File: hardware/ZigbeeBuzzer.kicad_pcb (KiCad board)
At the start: 2 copper layers, 26 x 21 mm, 14 parts, among them Q1 NPN, U1 Xiao-ESP32-C6

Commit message: Added diode
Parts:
- added D1: CUS08F30, Medo64:D Shottky (SOD123F), B.Cu at (41.5, 29.3)
- moved S1 1.50 mm to (41.5, 35.5)
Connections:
- U1 pad 10: (no net) -> BUTTON
- U1 pad 11: BUTTON -> (no net)
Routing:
- net BEEPER: track 18.0 -> 29.5 mm
- net GND: track 65.3 -> 71.3 mm, vias 1 -> 2
- net 3V3: track 39.7 -> 41.9 mm
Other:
- outline, holes or cut-outs redrawn

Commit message: Added PCB designator
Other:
- board text added: "ZigbeeBuzzer AXXXX"
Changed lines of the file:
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@@
 		(layer "F.Fab")
+	)
+	(gr_text "ZigbeeBuzzer AXXXX"
+		(at 33 33 0)
+		(layer "B.SilkS")
+		(effects
+			(font
+				(size 0.8 0.6)
+				(thickness 0.15)
+				(bold yes)
+			)
+			(justify mirror)
+		)
 	)
 	(segment

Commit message: Added polarity marking to beeper
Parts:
- turned LS1 to 90 degrees
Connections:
- LS1 pad 1: 3V3 -> BEEPER
- LS1 pad 2: BEEPER -> 3V3
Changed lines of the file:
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@@
 	(footprint "Medo64:LS Buzzer (D9.5-H5.5)"
 		(layer "B.Cu")
-		(at 33 26 -90)
+		(at 33 26 90)
 		(property "Reference" "LS1"
 			(at 0 0 0)
@@
 			(layer "B.Fab")
 		)
-		(pad "1" thru_hole circle
-			(at -2.5 0 270)
+		(fp_text user "+"
+			(at 2.5 1 90)
+			(layer "B.SilkS")
+			(effects
+				(font
+					(size 0.8 0.6)
+					(thickness 0.15)
+					(bold yes)
+				)
+				(justify top mirror)
+			)
+		)
+		(pad "1" thru_hole roundrect
+			(at -2.5 0 90)
+			(size 1.4 1.4)
+			(drill 0.8)
+			(layers "*.Cu" "*.Mask")
+			(remove_unused_layers no)
+			(roundrect_rratio 0.25)
+			(chamfer_ratio 0.2)
+			(chamfer top_left bottom_left)
+			(net 7 "BEEPER")
+		)
+		(pad "2" thru_hole circle
+			(at 2.5 0 90)
 			(size 1.4 1.4)
 			(drill 0.8)
@@
 			(net 8 "3V3")
 		)
-		(pad "2" thru_hole circle
-			(at 2.5 0 270)
-			(size 1.4 1.4)
-			(drill 0.8)
-			(layers "*.Cu" "*.Mask")
-			(remove_unused_layers no)
-			(net 7 "BEEPER")
-		)
 		(embedded_fonts no)

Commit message: Refactoring button location
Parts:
- moved DS1 13.5 mm to (33.0, 32.5), turned to 0 degrees
- moved S1 11.0 mm to (41.5, 24.5), turned to 90 degrees
- moved R4 10.7 mm to (41.5, 35.2), turned to 0 degrees
- moved D1 3.40 mm to (41.5, 32.7), turned to 180 degrees
- moved C2 3.40 mm to (41.5, 30.2)
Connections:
- R4 pad 1: (no net) -> OUT_LED
- U1 pad 9: (no net) -> OUT_LED
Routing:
- net LED: track 2.45 -> 9.60 mm
- net BUTTON: track 9.12 -> 16.1 mm
- net GND: track 71.3 -> 67.6 mm
- net BEEPER: track 29.5 -> 26.7 mm
- net OUT_LED: track 0.00 -> 2.71 mm, vias 0 -> 1
- net 3V3: track 41.9 -> 40.2 mm

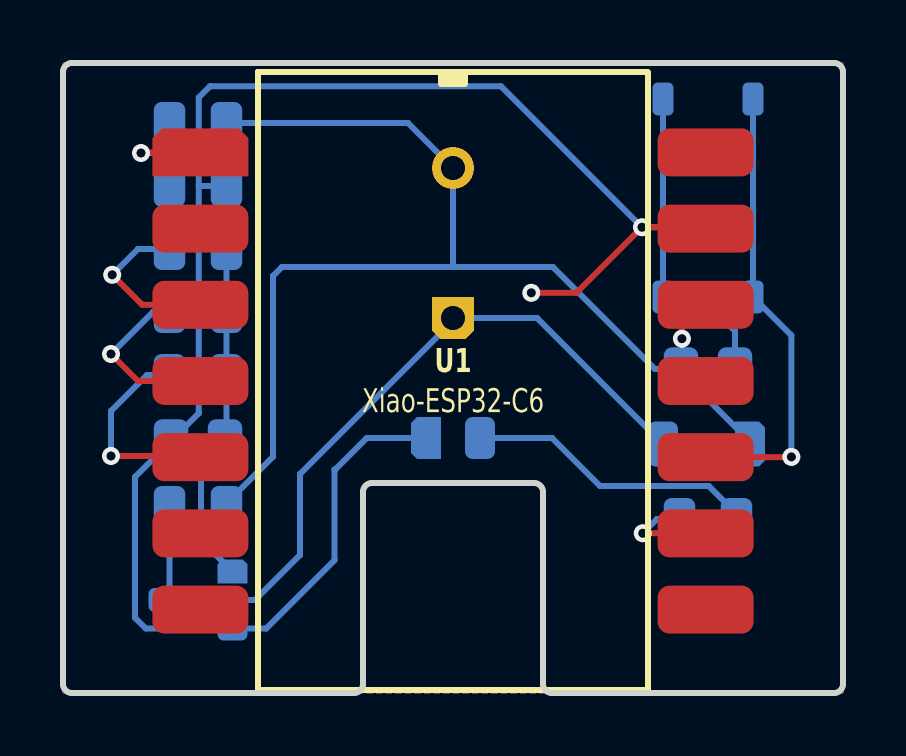
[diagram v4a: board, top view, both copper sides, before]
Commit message: Updated buzzer footprint
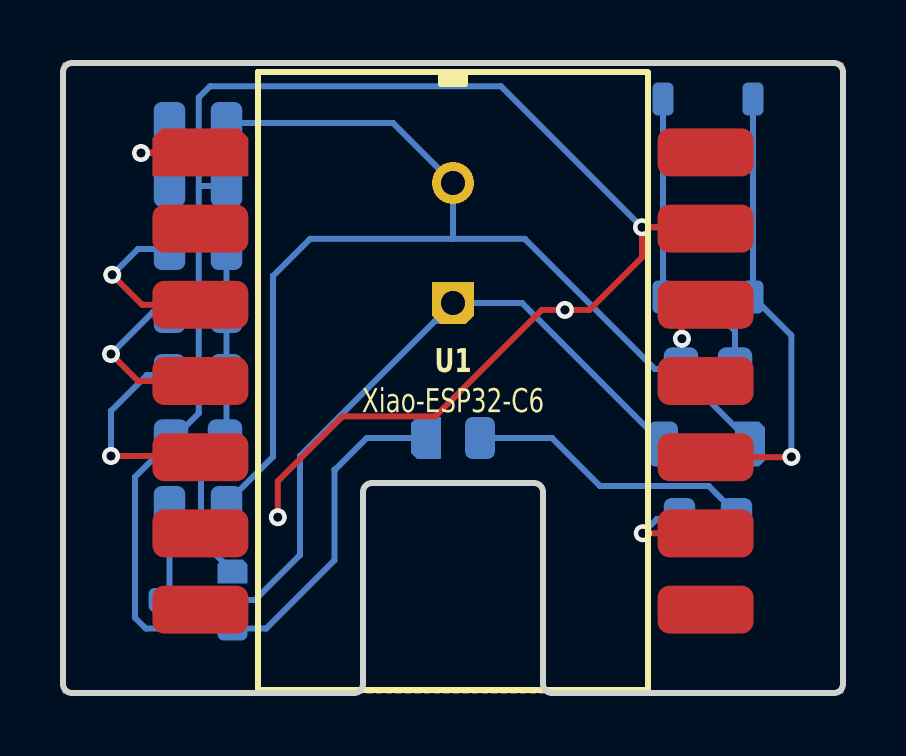
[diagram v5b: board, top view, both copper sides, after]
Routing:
- net GND: track 67.6 -> 80.4 mm, vias 2 -> 3
- net BEEPER: track 26.7 -> 27.3 mm
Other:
- board text added: "ZigbeeBuzzer BXXXX"
- board text removed: "ZigbeeBuzzer AXXXX"
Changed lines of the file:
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@@
 		(fp_circle
 			(center 0 0)
-			(end 4.6 0)
+			(end 4.4 0)
 			(stroke
 				(width 0.2)
@@
 		)
 		(pad "1" thru_hole roundrect
-			(at -2.5 0 90)
+			(at -2 0 90)
 			(size 1.4 1.4)
 			(drill 0.8)
@@
 		)
 		(pad "2" thru_hole circle
-			(at 2.5 0 90)
+			(at 2 0 90)
 			(size 1.4 1.4)
 			(drill 0.8)
@@
 		(model "${KICAD9_3DMODEL_DIR}/Buzzer_Beeper.3dshapes/Buzzer_15x7.5RM7.6.step"
 			(offset
-				(xyz -2.5 0 0)
+				(xyz -2 0 0)
 			)
 			(scale
-				(xyz 0.65 0.65 0.75)
+				(xyz 0.5 0.5 0.75)
 			)
 			(rotate
@@
 		(layer "F.Fab")
 	)
-	(gr_text "ZigbeeBuzzer AXXXX"
+	(gr_text "ZigbeeBuzzer BXXXX"
 		(at 29.1 35.8 90)
 		(layer "B.SilkS")
@@
 	)
 	(segment
+		(start 39.3 26.48)
+		(end 37.55 28.23)
+		(width 0.2)
+		(layer "F.Cu")
+		(net 1)
+	)
+	(segment
+		(start 36.73 28.23)
+		(end 35.96 28.23)
+		(width 0.2)
+		(layer "F.Cu")
+		(net 1)
+	)
+	(segment
+		(start 37.55 28.23)
+		(end 36.73 28.23)
+		(width 0.2)
+		(layer "F.Cu")
+		(net 1)
+	)
+	(segment
+		(start 27.16 33.94)
+		(end 27.16 35.14)
+		(width 0.2)
+		(layer "F.Cu")
+		(net 1)
+	)
+	(segment
 		(start 39.3 25.475)
-		(end 37.115 27.66)
+		(end 39.3 26.48)
+		(width 0.2)
+		(layer "F.Cu")
+		(net 1)
+	)
+	(segment
+		(start 29.32 31.78)
+		(end 27.16 33.94)
+		(width 0.2)
+		(layer "F.Cu")
+		(net 1)
+	)
+	(segment
+		(start 35.96 28.23)
+		(end 32.41 31.78)
+		(width 0.2)
+		(layer "F.Cu")
+		(net 1)
+	)
+	(segment
+		(start 32.41 31.78)
+		(end 29.32 31.78)
 		(width 0.2)
 		(layer "F.Cu")
@@
 		(start 39.3 25.475)
 		(end 40.575 25.475)
-		(width 0.2)
-		(layer "F.Cu")
-		(net 1)
-	)
-	(segment
-		(start 37.115 27.66)
-		(end 35.61 27.66)
 		(width 0.2)
 		(layer "F.Cu")
@@
 	)
 	(via
-		(at 35.61 27.66)
+		(at 27.16 35.14)
+		(size 0.6)
+		(drill 0.3)
+		(layers "F.Cu" "B.Cu")
+		(net 1)
+	)
+	(via
+		(at 36.73 28.23)
 		(size 0.6)
 		(drill 0.3)
@@
 	)
 	(segment
-		(start 40 32.7)
-		(end 35.8 28.5)
+		(start 27.9 36.4)
+		(end 27.9 33.1)
+		(width 0.2)
+		(layer "B.Cu")
+		(net 7)
+	)
+	(segment
+		(start 35.3 28)
+		(end 33 28)
+		(width 0.2)
+		(layer "B.Cu")
+		(net 7)
+	)
+	(segment
+		(start 27.9 33.1)
+		(end 32.4 28.6)
 		(width 0.2)
 		(layer "B.Cu")
@@
 	)
 	(segment
+		(start 32.4 28.6)
+		(end 33 28.6)
+		(width 0.2)
+		(layer "B.Cu")
+		(net 7)
+	)
+	(segment
+		(start 23.55 34.8)
+		(end 23.55 37.7)
+		(width 0.2)
+		(layer "B.Cu")
+		(net 7)
+	)
+	(segment
+		(start 40 32.7)
+		(end 35.3 28)
+		(width 0.2)
+		(layer "B.Cu")
+		(net 7)
+	)
+	(segment
 		(start 23.35 37.9)
 		(end 26.4 37.9)
-		(width 0.2)
-		(layer "B.Cu")
-		(net 7)
-	)
-	(segment
-		(start 35.8 28.5)
-		(end 33 28.5)
-		(width 0.2)
-		(layer "B.Cu")
-		(net 7)
-	)
-	(segment
-		(start 27.9 33.7)
-		(end 33 28.6)
-		(width 0.2)
-		(layer "B.Cu")
-		(net 7)
-	)
-	(segment
-		(start 27.9 36.4)
-		(end 27.9 33.7)
-		(width 0.2)
-		(layer "B.Cu")
-		(net 7)
-	)
-	(segment
-		(start 23.55 34.8)
-		(end 23.55 37.7)
 		(width 0.2)
 		(layer "B.Cu")
@@
 	)
 	(segment
+		(start 35.39 25.86)
+		(end 33 25.86)
+		(width 0.2)
+		(layer "B.Cu")
+		(net 8)
+	)
+	(segment
+		(start 39.73 30.2)
+		(end 35.39 25.86)
+		(width 0.2)
+		(layer "B.Cu")
+		(net 8)
+	)
+	(segment
+		(start 27 33.125)
+		(end 27 27.1)
+		(width 0.2)
+		(layer "B.Cu")
+		(net 8)
+	)
+	(segment
+		(start 40.6 30.2)
+		(end 39.73 30.2)
+		(width 0.2)
+		(layer "B.Cu")
+		(net 8)
+	)
+	(segment
+		(start 27 27.1)
+		(end 28.24 25.86)
+		(width 0.2)
+		(layer "B.Cu")
+		(net 8)
+	)
+	(segment
+		(start 31 22)
+		(end 33 24)
+		(width 0.2)
+		(layer "B.Cu")
+		(net 8)
+	)
+	(segment
+		(start 33 24)
+		(end 33 25.86)
+		(width 0.2)
+		(layer "B.Cu")
+		(net 8)
+	)
+	(segment
 		(start 25.45 22)
-		(end 31.5 22)
+		(end 31 22)
 		(width 0.2)
 		(layer "B.Cu")
@@
 	)
 	(segment
-		(start 39.73 30.2)
-		(end 36.33 26.8)
-		(width 0.2)
-		(layer "B.Cu")
-		(net 8)
-	)
-	(segment
-		(start 33 23.5)
-		(end 33 26.8)
-		(width 0.2)
-		(layer "B.Cu")
-		(net 8)
-	)
-	(segment
-		(start 31.5 22)
-		(end 33 23.5)
+		(start 28.24 25.86)
+		(end 33 25.86)
 		(width 0.2)
 		(layer "B.Cu")
@@
 	)
 	(segment
-		(start 27.3 26.8)
-		(end 33 26.8)
-		(width 0.2)
-		(layer "B.Cu")
-		(net 8)
-	)
-	(segment
-		(start 27 27.1)
-		(end 27.3 26.8)
-		(width 0.2)
-		(layer "B.Cu")
-		(net 8)
-	)
-	(segment
 		(start 25.45 34.675)
 		(end 27 33.125)
 		(width 0.2)
 		(layer "B.Cu")
-		(net 8)
-	)
-	(segment
-		(start 36.33 26.8)
-		(end 33 26.8)
-		(width 0.2)
-		(layer "B.Cu")
-		(net 8)
-	)
-	(segment
-		(start 27 33.125)
-		(end 27 27.1)
-		(width 0.2)
-		(layer "B.Cu")
-		(net 8)
-	)
-	(segment
-		(start 40.6 30.2)
-		(end 39.73 30.2)
-		(width 0.2)
-		(layer "B.Cu")
